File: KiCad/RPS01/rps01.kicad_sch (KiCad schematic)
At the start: 8 parts, among them J1 XT90 BAT1, J2 XT90 BAT2, J3 XT90 ESC Output, J4 XT30PW Horizontal, J5 MCU_prog_header, J6 MCU_ICSP_header, J7 MCU_I2C_JSTGH3, U9 5V_500MA_REG

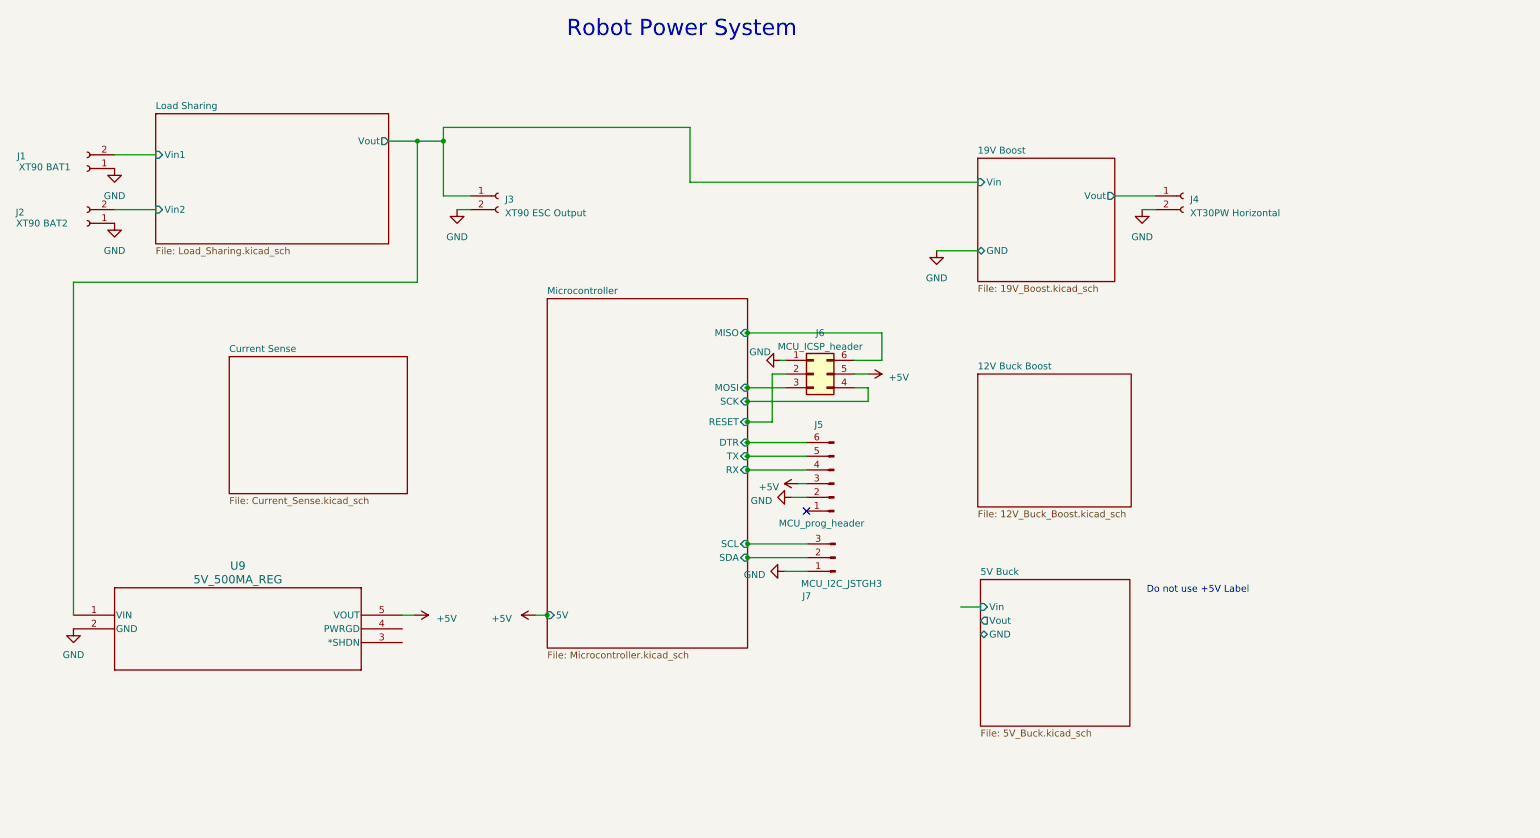
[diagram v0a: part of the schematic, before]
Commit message: Root cleanup and new regulator
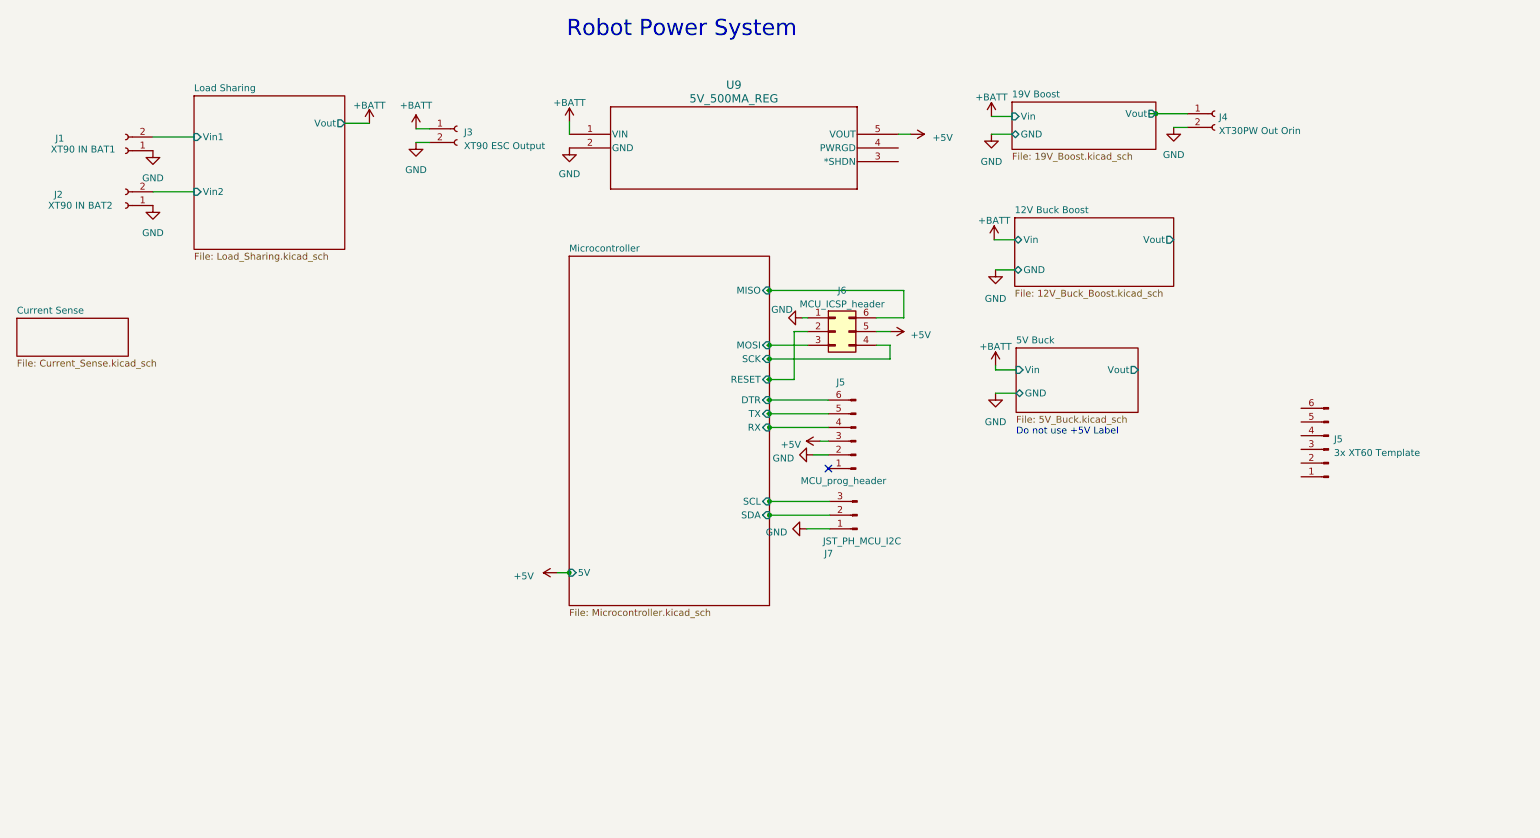
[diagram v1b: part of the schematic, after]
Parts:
- added J5: 3x XT60 Template, symbol Connector:Conn_01x06_Pin
- J1: value XT90 BAT1 -> XT90 IN BAT1
- J2: value XT90 BAT2 -> XT90 IN BAT2
- J4: value XT30PW Horizontal -> XT30PW Out Orin
- J7: value MCU_I2C_JSTGH3 -> JST_PH_MCU_I2C
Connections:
- net 19V Boost/Vin renamed +BATT
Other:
- sheet 12V Buck Boost ports: added GND, Vin, Vout; removed none
- moved on the sheet: J1, J2, J3, J4, J5, J6, J7, U9

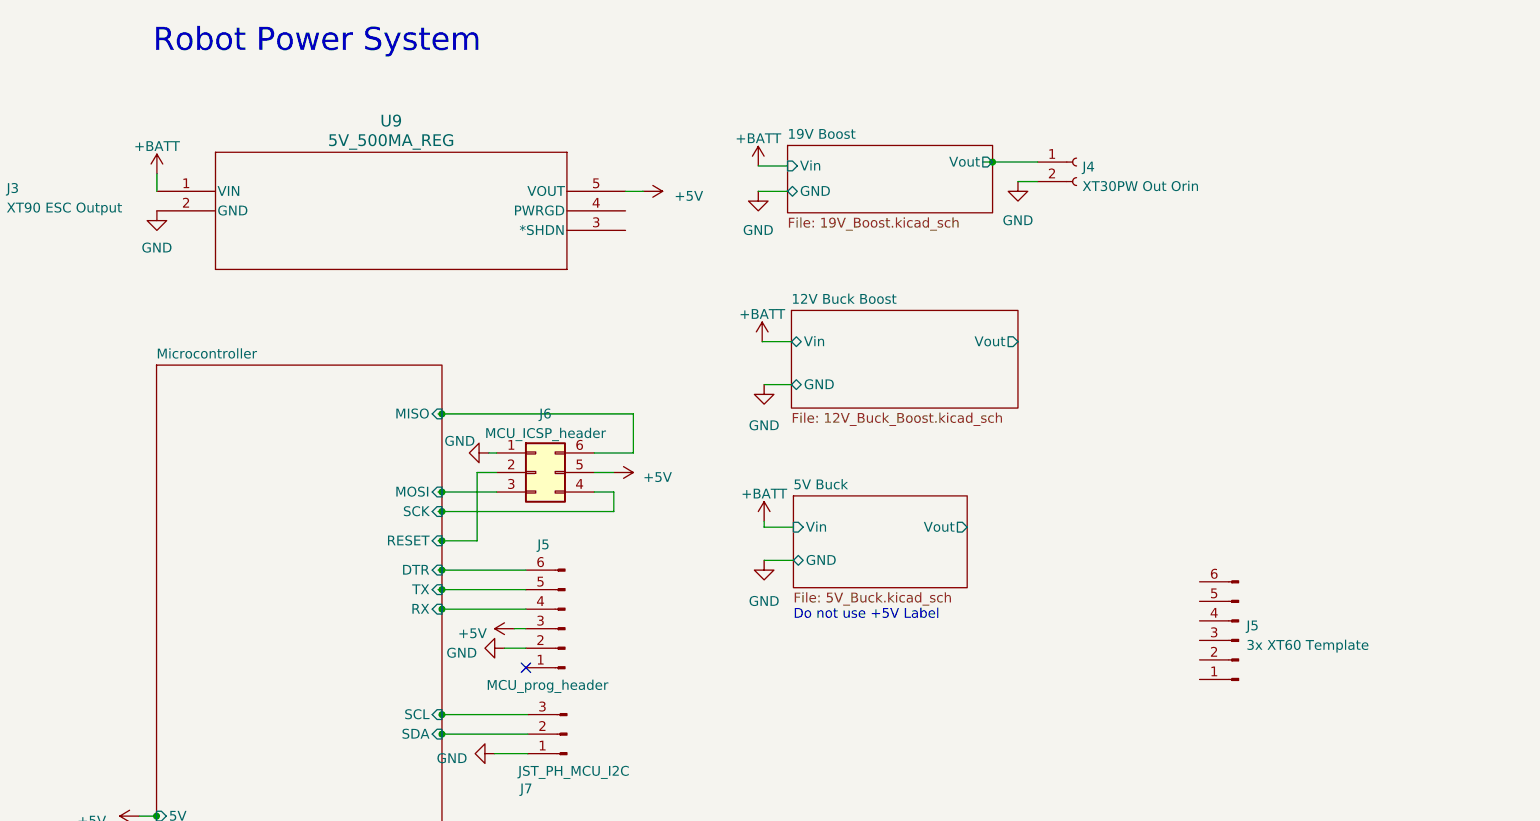
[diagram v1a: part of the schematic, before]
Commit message: Net listed and attacked outline components
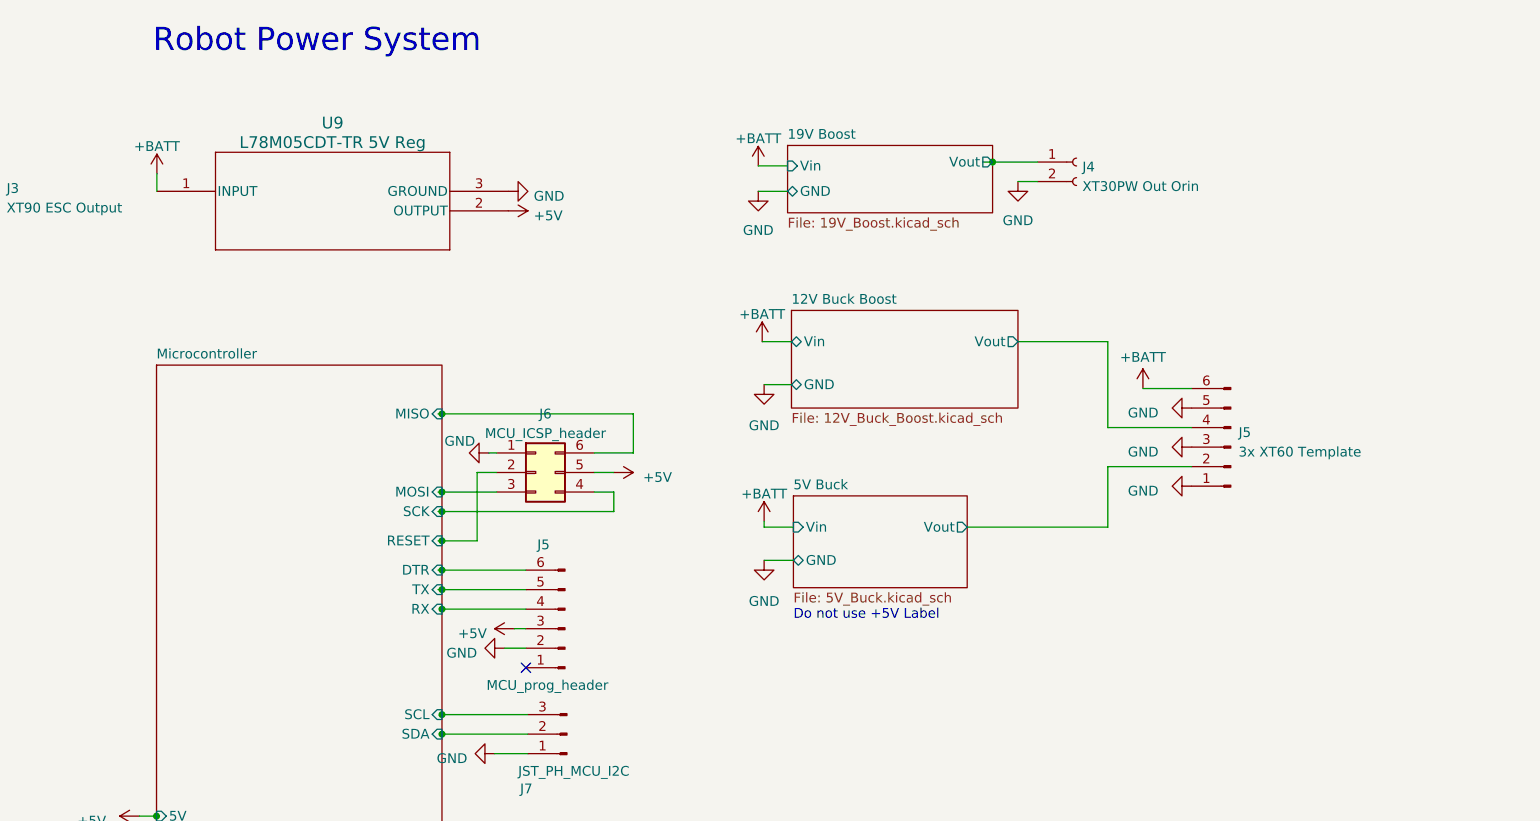
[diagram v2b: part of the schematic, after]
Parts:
- removed U9: 5V_500MA_REG, Mechatronics 5VReg:SOT-23-5_MC_MCH, symbol 5V_500mA_Reg:MCP1755T-5002E_OT
- added U9: L78M05CDT-TR 5V Reg, Mechatronics 5V Reg:DPAK_STM, symbol 5V Regulator:L78M05CDT-TR
- J5: footprint (none) -> Mechatronics Template:V0_PC100_Power_Board
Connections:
- net +5V: now also U9.2 (OUTPUT)
- net +BATT: now also J5.6 (Pin_6), U9.1 (INPUT)
- net 12V Buck Boost/Vout: now also J5.4 (Pin_4)
- net 5V Buck/Vout: now also J5.2 (Pin_2)
- net GND: now also J5.1 (Pin_1), J5.3 (Pin_3), J5.5 (Pin_5), U9.3 (GROUND)
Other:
- moved on the sheet: J5

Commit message: Changed footprints on my end only
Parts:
- J1, J2: footprint Mechatronic Footprints:AMASS_XT90-F_1x02_P11.00mm_Vertical -> Mechatronics AMASS XT90 Vertical:AMASS_XT90-M_1x02_P11.00mm_Vertical
- J3: footprint AMASS XT90 Vertical:AMASS_XT90-M_1x02_P11.00mm_Vertical -> Mechatronics AMASS XT90 Vertical:AMASS_XT90-F_1x02_P11.00mm_Vertical
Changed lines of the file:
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@@
       (effects (font (size 1.27 1.27)))
     )
-    (property "Footprint" "Mechatronic Footprints:AMASS_XT90-F_1x02_P11.00mm_Vertical" (at 42.672 50.038 0)
+    (property "Footprint" "Mechatronics AMASS XT90 Vertical:AMASS_XT90-M_1x02_P11.00mm_Vertical" (at 42.672 50.038 0)
       (effects (font (size 1.27 1.27)) hide)
     )
@@
       (effects (font (size 1.27 1.27)))
     )
-    (property "Footprint" "Mechatronic Footprints:AMASS_XT90-F_1x02_P11.00mm_Vertical" (at 42.672 39.878 0)
+    (property "Footprint" "Mechatronics AMASS XT90 Vertical:AMASS_XT90-M_1x02_P11.00mm_Vertical" (at 42.672 39.878 0)
       (effects (font (size 1.27 1.27)) hide)
     )
@@
       (effects (font (size 1.27 1.27)) (justify left))
     )
-    (property "Footprint" "AMASS XT90 Vertical:AMASS_XT90-M_1x02_P11.00mm_Vertical" (at 104.14 35.814 0)
-      (effects (font (size 1.27 1.27)) hide)
-    )
+    (property "Footprint" "Mechatronics AMASS XT90 Vertical:AMASS_XT90-F_1x02_P11.00mm_Vertical" (at 104.14 35.814 0)
+      (effects (font (size 1.27 1.27)) hide)
+    )

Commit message: update for layout before 1 H break
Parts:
- J4: footprint Connector_AMASS:AMASS_XT60-F_1x02_P7.20mm_Vertical -> Connector_AMASS:AMASS_XT30PW-F_1x02_P2.50mm_Horizontal
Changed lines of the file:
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@@
       (effects (font (size 1.27 1.27)) (justify left))
     )
-    (property "Footprint" "Connector_AMASS:AMASS_XT60-F_1x02_P7.20mm_Vertical" (at 244.602 33.02 0)
+    (property "Footprint" "Connector_AMASS:AMASS_XT30PW-F_1x02_P2.50mm_Horizontal" (at 244.602 33.02 0)
       (effects (font (size 1.27 1.27)) hide)
     )

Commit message: Layout Updates
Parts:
- added J6: XT30PW Bat Out, Connector_AMASS:AMASS_XT30PW-F_1x02_P2.50mm_Horizontal, symbol Connector:Conn_01x02_Pin
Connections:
- net +BATT: now also J6.2 (Pin_2)
- net GND: now also J6.1 (Pin_1)
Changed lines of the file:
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@@
     (stroke (width 0) (type default))
   )
+  (wire (pts (xy 96.647 50.1904) (xy 97.9424 50.1904))
+    (stroke (width 0) (type default))
+  )
   (wire (pts (xy 230.378 80.518) (xy 248.666 80.518))
     (stroke (width 0) (type default))
@@
     (data
       iVBORw0KGgoAAAANSUhEUgAABSIAAALqCAIAAACuVr0nAAAAA3NCSVQICAjb4U/gAAAACXBIWXMA
-      AB2HAAAdhwGP5fFlAAAgAElEQVR4nOy9Z3xVVdo+vPY+PQ1CCGWkFyPSQ5UOShNQREVRHxRwwC62
+      AB1MAAAdTAHcxBGXAAAgAElEQVR4nOy9Z3xVVdo+vPY+PQ1CCGWkFyPSQ5UOShNQREVRHxRwwC62
       wVGYUXRQUMTyAx3F3gVmpApKCaDSQ4shCSVSDCUJgbTTz34/XM++3pWT5BAyifP8Z9b1gd/JOXuv
       vcq9Nve17qYZhiEUFBQUFBQUFBQUFBQUFBRqAvq/uwMKCgoKCgoKCgoKCgoKCv85UDRbQUFBQUFB
@@
     )
   )
+  (symbol (lib_id "power:GND") (at 97.9424 52.7304 0) (unit 1)
+    (in_bom yes) (on_board yes) (dnp no) (fields_autoplaced)
+    (property "Reference" "#PWR077" (at 97.9424 59.0804 0)
+      (effects (font (size 1.27 1.27)) hide)
+    )
+    (property "Value" "GND" (at 97.9424 58.42 0)
+      (effects (font (size 1.27 1.27)))
+    )
+    (property "Footprint" "" (at 97.9424 52.7304 0)
+      (effects (font (size 1.27 1.27)) hide)
+    )
+    (property "Datasheet" "" (at 97.9424 52.7304 0)
+      (effects (font (size 1.27 1.27)) hide)
+    )
+    (pin "1")
+    (instances
+      (project "rps01"
+        (path "/14930f15-c0a0-4b55-93e6-b112548415f6"
+          (reference "#PWR077") (unit 1)
+        )
+      )
+    )
+  )
+  (symbol (lib_id "power:+BATT") (at 96.647 50.1904 0) (unit 1)
+    (in_bom yes) (on_board yes) (dnp no) (fields_autoplaced)
+    (property "Reference" "#PWR078" (at 96.647 54.0004 0)
+      (effects (font (size 1.27 1.27)) hide)
+    )
+    (property "Value" "+BATT" (at 96.647 46.99 0)
+      (effects (font (size 1.27 1.27)))
+    )
+    (property "Footprint" "" (at 96.647 50.1904 0)
+      (effects (font (size 1.27 1.27)) hide)
+    )
+    (property "Datasheet" "" (at 96.647 50.1904 0)
+      (effects (font (size 1.27 1.27)) hide)
+    )
+    (pin "1")
+    (instances
+      (project "rps01"
+        (path "/14930f15-c0a0-4b55-93e6-b112548415f6"
+          (reference "#PWR078") (unit 1)
+        )
+      )
+    )
+  )
   (symbol (lib_id "power:+BATT") (at 203.2 33.528 0) (unit 1)
     (in_bom yes) (on_board yes) (dnp no) (fields_autoplaced)
@@
         )
       )
+    )
+  )
+  (symbol (lib_id "Connector:Conn_01x02_Pin") (at 103.0224 52.7304 180) (unit 1)
+    (in_bom yes) (on_board yes) (dnp no) (fields_autoplaced)
+    (property "Reference" "J6" (at 104.14 50.8254 0)
+      (effects (font (size 1.27 1.27)) (justify right))
+    )
+    (property "Value" "XT30PW Bat Out" (at 104.14 53.3654 0)
+      (effects (font (size 1.27 1.27)) (justify right))
+    )
+    (property "Footprint" "Connector_AMASS:AMASS_XT30PW-F_1x02_P2.50mm_Horizontal" (at 103.0224 52.7304 0)
+      (effects (font (size 1.27 1.27)) hide)
+    )
+    (property "Datasheet" "~" (at 103.0224 52.7304 0)
+      (effects (font (size 1.27 1.27)) hide)
+    )
+    (pin "1")
+    (pin "2")
+    (instances
+      (project "rps01"
+        (path "/14930f15-c0a0-4b55-93e6-b112548415f6"
+          (reference "J6") (unit 1)
+        )
+      )

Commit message: All Footprints Load from Mechatronics Folder
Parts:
- J1, J2: footprint Mechatronics AMASS XT90 Vertical:AMASS_XT90-M_1x02_P11.00mm_Vertical -> Mechatronic Footprints:AMASS_XT90-M_1x02_P11.00mm_Vertical
- J3: footprint Mechatronics AMASS XT90 Vertical:AMASS_XT90-F_1x02_P11.00mm_Vertical -> Mechatronic Footprints:AMASS_XT90-F_1x02_P11.00mm_Vertical
- J5: footprint Mechatronics Template:V0_PC100_Power_Board -> Mechatronic Footprints:V0_PC100_Power_Board
- U9: footprint Mechatronics 5V Reg:DPAK_STM -> Mechatronic Footprints:5V_REGULATOR_DPAK_STM
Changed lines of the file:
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@@
       (effects (font (size 1.27 1.27)) (justify right))
     )
-    (property "Footprint" "Mechatronics Template:V0_PC100_Power_Board" (at 264.668 70.104 0)
+    (property "Footprint" "Mechatronic Footprints:V0_PC100_Power_Board" (at 264.668 70.104 0)
       (effects (font (size 1.27 1.27)) hide)
     )
@@
       (effects (font (size 1.27 1.27)))
     )
-    (property "Footprint" "Mechatronics AMASS XT90 Vertical:AMASS_XT90-M_1x02_P11.00mm_Vertical" (at 42.672 50.038 0)
+    (property "Footprint" "Mechatronic Footprints:AMASS_XT90-M_1x02_P11.00mm_Vertical" (at 42.672 50.038 0)
       (effects (font (size 1.27 1.27)) hide)
     )
@@
       (effects (font (size 1.524 1.524)))
     )
-    (property "Footprint" "Mechatronics 5V Reg:DPAK_STM" (at 124.968 36.83 0)
+    (property "Footprint" "Mechatronic Footprints:5V_REGULATOR_DPAK_STM" (at 124.968 36.83 0)
       (effects (font (size 1.27 1.27) italic) hide)
     )
@@
       (effects (font (size 1.27 1.27)))
     )
-    (property "Footprint" "Mechatronics AMASS XT90 Vertical:AMASS_XT90-M_1x02_P11.00mm_Vertical" (at 42.672 39.878 0)
+    (property "Footprint" "Mechatronic Footprints:AMASS_XT90-M_1x02_P11.00mm_Vertical" (at 42.672 39.878 0)
       (effects (font (size 1.27 1.27)) hide)
     )
@@
       (effects (font (size 1.27 1.27)) (justify left))
     )
-    (property "Footprint" "Mechatronics AMASS XT90 Vertical:AMASS_XT90-F_1x02_P11.00mm_Vertical" (at 104.14 35.814 0)
-      (effects (font (size 1.27 1.27)) hide)
-    )
+    (property "Footprint" "Mechatronic Footprints:AMASS_XT90-F_1x02_P11.00mm_Vertical" (at 104.14 35.814 0)
+      (effects (font (size 1.27 1.27)) hide)
+    )

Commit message: Progress saving on Load Sharing
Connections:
- net +BATT: now also J3.2 (Pin_2); no longer J3.1 (Pin_1)
- net GND: now also J3.1 (Pin_1); no longer J3.2 (Pin_2)
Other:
- moved on the sheet: J3
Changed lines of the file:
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@@
     (stroke (width 0) (type default))
   )
+  (wire (pts (xy 97.7138 35.814) (xy 96.52 35.814))
+    (stroke (width 0) (type default))
+  )
   (wire (pts (xy 203.962 80.518) (xy 203.962 79.756))
     (stroke (width 0) (type default))
@@
     (stroke (width 0) (type default))
   )
-  (wire (pts (xy 96.52 35.814) (xy 99.06 35.814))
-    (stroke (width 0) (type default))
-  )
   (wire (pts (xy 203.962 61.976) (xy 207.518 61.976))
     (stroke (width 0) (type default))
@@
     (stroke (width 0) (type default))
   )
-  (wire (pts (xy 99.06 38.354) (xy 96.52 38.354))
-    (stroke (width 0) (type default))
-  )
   (wire (pts (xy 168.91 109.982) (xy 173.228 109.982))
     (stroke (width 0) (type default))
@@
     (stroke (width 0) (type default))
   )
+  (wire (pts (xy 97.7138 38.354) (xy 96.52 38.354))
+    (stroke (width 0) (type default))
+  )
   (image (at 87.122 170.942) (scale 0.532729)
     (data
@@
     )
   )
-  (symbol (lib_id "Connector:Conn_01x02_Socket") (at 104.14 35.814 0) (unit 1)
-    (in_bom yes) (on_board yes) (dnp no) (fields_autoplaced)
-    (property "Reference" "J3" (at 105.41 36.449 0)
+  (symbol (lib_id "Connector:Conn_01x02_Socket") (at 102.7938 38.354 0) (mirror x) (unit 1)
+    (in_bom yes) (on_board yes) (dnp no)
+    (property "Reference" "J3" (at 104.0638 37.719 0)
       (effects (font (size 1.27 1.27)) (justify left))
     )
-    (property "Value" "XT90 ESC Output" (at 105.41 38.989 0)
+    (property "Value" "XT90 ESC Output" (at 104.0638 35.179 0)
       (effects (font (size 1.27 1.27)) (justify left))
     )
-    (property "Footprint" "Mechatronic Footprints:AMASS_XT90-F_1x02_P11.00mm_Vertical" (at 104.14 35.814 0)
+    (property "Footprint" "Mechatronic Footprints:AMASS_XT90-F_1x02_P11.00mm_Vertical" (at 102.7938 38.354 0)
       (effects (font (size 1.27 1.27)) hide)
     )
-    (property "Datasheet" "~" (at 104.14 35.814 0)
+    (property "Datasheet" "~" (at 102.7938 38.354 0)
       (effects (font (size 1.27 1.27)) hide)
     )
